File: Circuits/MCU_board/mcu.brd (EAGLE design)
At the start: 80 x 70 mm, 78 parts, among them IC1 RP111N331B-TR-FE, IC2 FT230XS, U1 TCA9548APWR, U2 USBLC6-2P6, U4 LSM9DS1, U5 STM32L452RECT6

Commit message: Separate a couple of MCU traces to use separate vias to avoid potential loop
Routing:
- net GND: track 143.2 -> 137.7 mm, vias 17 -> 18
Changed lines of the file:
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@@
 <?xml version="1.0" encoding="utf-8"?>
 <!DOCTYPE eagle SYSTEM "eagle.dtd">
-<eagle version="9.4.2">
+<eagle version="9.3.2">
 <drawing>
 <settings>
@@
 <attribute name="MEM" value="" x="61.4022" y="35.0262" size="1.778" layer="27" display="off"/>
 <attribute name="MFPN" value="STM32L476RCT6" x="61.4022" y="35.0262" size="1.778" layer="27" display="off"/>
+<attribute name="NAME" x="41.0822" y="44.5462" size="0.8128" layer="151" ratio="10" align="center"/>
 <attribute name="NAME" x="36.8822" y="48.1462" size="1.016" layer="25" font="vector" ratio="18" align="bottom-right"/>
-<attribute name="NAME" x="41.0822" y="44.5462" size="0.8128" layer="151" ratio="10" align="center"/>
 <attribute name="PARTNO" value="" x="61.4022" y="35.0262" size="1.778" layer="27" display="off"/>
 <attribute name="STATUS" value="" x="61.4022" y="35.0262" size="1.778" layer="27" display="off"/>
@@
 <wire x1="14.4726" y1="53.163" x2="16.687" y2="53.163" width="0.3048" layer="1"/>
 <wire x1="16.687" y1="53.163" x2="16.6878" y2="53.1622" width="0.1524" layer="1"/>
-<via x="41.0972" y="34.0106" extent="1-16" drill="0.35"/>
-<wire x1="44.3322" y1="36.8962" x2="44.3322" y2="34.8326" width="0.3048" layer="1"/>
-<wire x1="44.3322" y1="34.8326" x2="43.5102" y2="34.0106" width="0.3048" layer="1"/>
-<wire x1="41.0972" y1="34.0106" x2="43.5102" y2="34.0106" width="0.3048" layer="1"/>
+<via x="44.3322" y="33.9852" extent="1-16" drill="0.35"/>
 <wire x1="57.6084" y1="35.2672" x2="57.6084" y2="33.3768" width="0.3048" layer="1"/>
 <wire x1="57.6084" y1="33.3768" x2="57.6072" y2="33.3756" width="0.1524" layer="1"/>
@@
 <wire x1="21.4046" y1="29.4873" x2="19.0521" y2="29.4873" width="0.3048" layer="1"/>
 <wire x1="19.0521" y1="29.4873" x2="19.05" y2="29.4894" width="0.1524" layer="1"/>
-<wire x1="37.8322" y1="36.8962" x2="37.8322" y2="34.761" width="0.3048" layer="1"/>
-<wire x1="37.8322" y1="34.761" x2="38.5826" y2="34.0106" width="0.3048" layer="1"/>
-<wire x1="38.5826" y1="34.0106" x2="41.0972" y2="34.0106" width="0.3048" layer="1"/>
 <wire x1="42.8954" y1="25.3306" x2="42.8752" y2="25.3104" width="0.1524" layer="1"/>
 <wire x1="42.8752" y1="25.3104" x2="42.8752" y2="22.4028" width="0.3048" layer="1"/>
@@
 <wire x1="70.0532" y1="17.9832" x2="72.93233125" y2="18.5018375" width="0.3048" layer="1"/>
 <wire x1="69.84200625" y1="73.107125" x2="69.4182" y2="70.7898" width="0.3048" layer="1"/>
+<wire x1="44.3322" y1="36.8962" x2="44.3322" y2="33.9852" width="0.3048" layer="1"/>
+<via x="37.8322" y="33.9852" extent="1-16" drill="0.35"/>
+<wire x1="37.8322" y1="36.8962" x2="37.8322" y2="33.9852" width="0.3048" layer="1"/>
 </signal>
 <signal name="SWDIO">

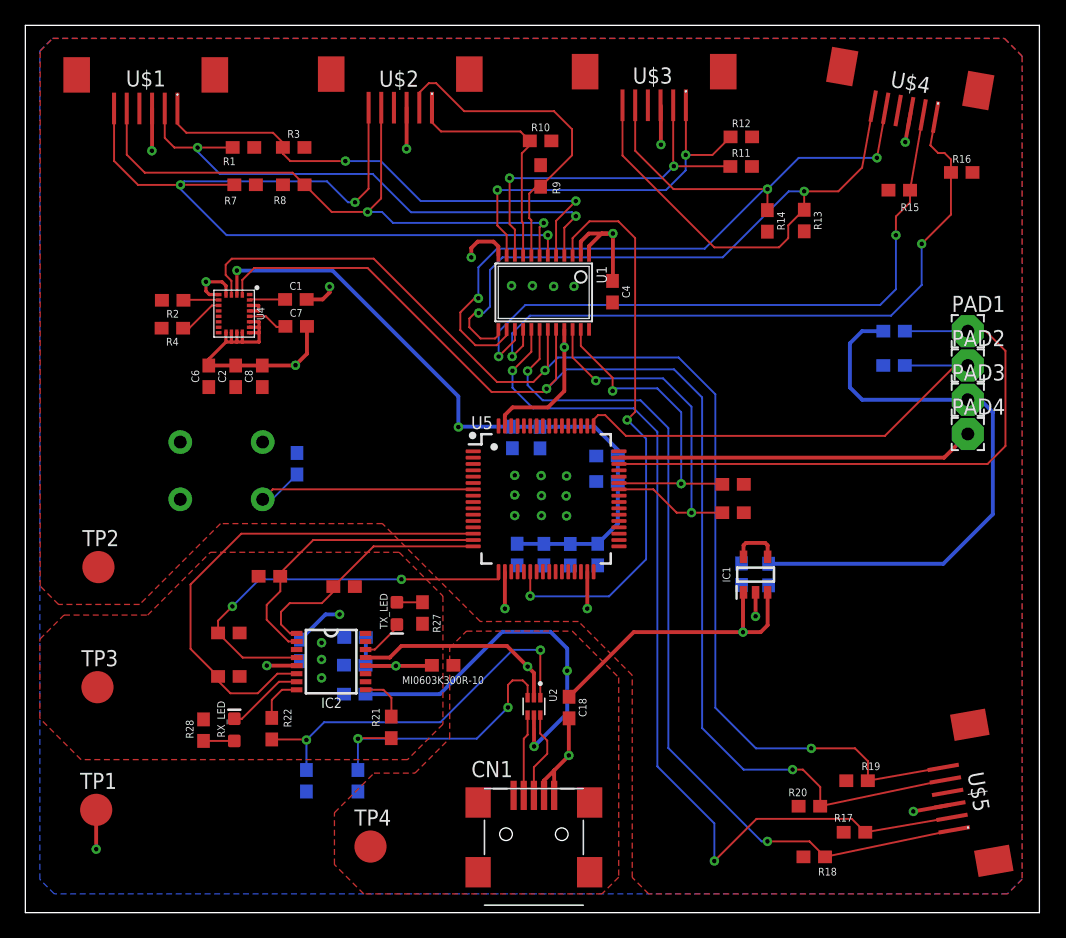
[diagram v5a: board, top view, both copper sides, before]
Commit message: Fixed silkscreen of components, Changed VCCIO plane
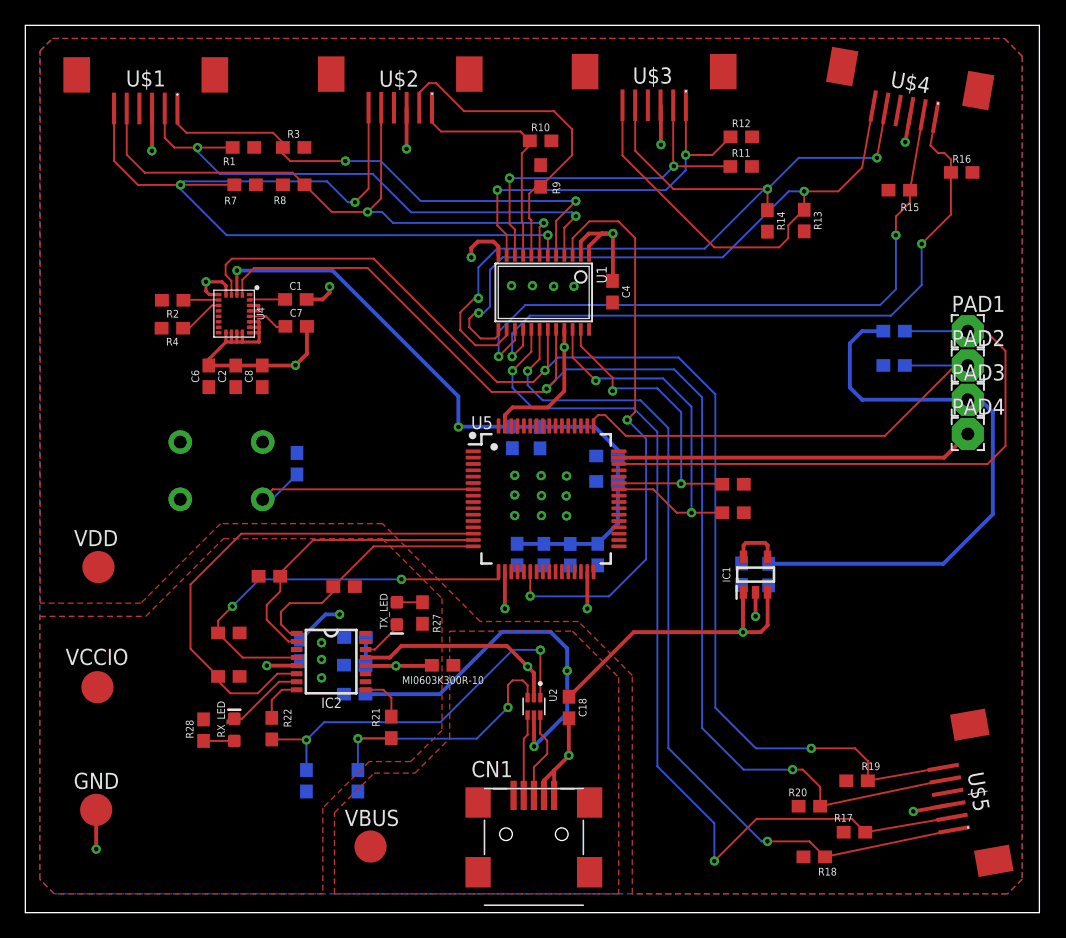
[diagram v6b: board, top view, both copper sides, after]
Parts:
- renumbered TP1 to GND, TP2 to VDD, TP3 to VCCIO, TP4 to VBUS
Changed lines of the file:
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@@
 <?xml version="1.0" encoding="utf-8"?>
 <!DOCTYPE eagle SYSTEM "eagle.dtd">
-<eagle version="9.3.2">
+<eagle version="9.4.2">
 <drawing>
 <settings>
@@
 <attribute name="MEM" value="" x="61.4022" y="35.0262" size="1.778" layer="27" display="off"/>
 <attribute name="MFPN" value="STM32L476RCT6" x="61.4022" y="35.0262" size="1.778" layer="27" display="off"/>
+<attribute name="NAME" x="36.8822" y="48.1462" size="1.016" layer="25" font="vector" ratio="18" align="bottom-right"/>
 <attribute name="NAME" x="41.0822" y="44.5462" size="0.8128" layer="151" ratio="10" align="center"/>
-<attribute name="NAME" x="36.8822" y="48.1462" size="1.016" layer="25" font="vector" ratio="18" align="bottom-right"/>
 <attribute name="PARTNO" value="" x="61.4022" y="35.0262" size="1.778" layer="27" display="off"/>
 <attribute name="STATUS" value="" x="61.4022" y="35.0262" size="1.778" layer="27" display="off"/>
@@
 <attribute name="VALUE" x="55.8292" y="43.0276" size="0.6096" layer="27" font="vector" ratio="20" align="top-center"/>
 </element>
-<element name="TP1" library="testpad" library_urn="urn:adsk.eagle:library:385" package="B2,54" package3d_urn="urn:adsk.eagle:package:27948/1" value="TPB2,54" x="5.588" y="18.1102" smashed="yes">
-<attribute name="NAME" x="4.318" y="19.7612" size="1.27" layer="25" ratio="10"/>
+<element name="GND" library="testpad" library_urn="urn:adsk.eagle:library:385" package="B2,54" package3d_urn="urn:adsk.eagle:package:27948/1" value="TPB2,54" x="5.588" y="18.1102" smashed="yes">
+<attribute name="NAME" x="3.81" y="19.7612" size="1.27" layer="25" ratio="10"/>
 <attribute name="TP_SIGNAL_NAME" value="" x="5.588" y="18.1102" size="1.778" layer="27" display="off"/>
 <attribute name="VALUE" x="4.318" y="16.7132" size="0.0254" layer="27"/>
 </element>
-<element name="TP2" library="testpad" library_urn="urn:adsk.eagle:library:385" package="B2,54" package3d_urn="urn:adsk.eagle:package:27948/1" value="TPB2,54" x="5.7658" y="37.2618" smashed="yes">
-<attribute name="NAME" x="4.4958" y="38.9128" size="1.27" layer="25" ratio="10"/>
+<element name="VDD" library="testpad" library_urn="urn:adsk.eagle:library:385" package="B2,54" package3d_urn="urn:adsk.eagle:package:27948/1" value="TPB2,54" x="5.7658" y="37.2618" smashed="yes">
+<attribute name="NAME" x="3.8354" y="38.9128" size="1.27" layer="25" ratio="10"/>
 <attribute name="TP_SIGNAL_NAME" value="" x="5.7658" y="37.2618" size="1.778" layer="27" display="off"/>
 <attribute name="VALUE" x="4.4958" y="35.8648" size="0.0254" layer="27"/>
 </element>
-<element name="TP3" library="testpad" library_urn="urn:adsk.eagle:library:385" package="B2,54" package3d_urn="urn:adsk.eagle:package:27948/1" value="TPB2,54" x="5.6896" y="27.7876" smashed="yes">
-<attribute name="NAME" x="4.4196" y="29.4386" size="1.27" layer="25" ratio="10"/>
+<element name="VCCIO" library="testpad" library_urn="urn:adsk.eagle:library:385" package="B2,54" package3d_urn="urn:adsk.eagle:package:27948/1" value="TPB2,54" x="5.6896" y="27.7876" smashed="yes">
+<attribute name="NAME" x="3.175" y="29.5402" size="1.27" layer="25" ratio="10"/>
 <attribute name="TP_SIGNAL_NAME" value="" x="5.6896" y="27.7876" size="1.778" layer="27" display="off"/>
 <attribute name="VALUE" x="4.4196" y="26.3906" size="0.0254" layer="27"/>
 </element>
-<element name="TP4" library="testpad" library_urn="urn:adsk.eagle:library:385" package="B2,54" package3d_urn="urn:adsk.eagle:package:27948/1" value="TPB2,54" x="27.2288" y="15.2146" smashed="yes">
-<attribute name="NAME" x="25.9588" y="16.8656" size="1.27" layer="25" ratio="10"/>
+<element name="VBUS" library="testpad" library_urn="urn:adsk.eagle:library:385" package="B2,54" package3d_urn="urn:adsk.eagle:package:27948/1" value="TPB2,54" x="27.2288" y="15.2146" smashed="yes">
+<attribute name="NAME" x="25.1968" y="16.8402" size="1.27" layer="25" ratio="10"/>
 <attribute name="TP_SIGNAL_NAME" value="" x="27.2288" y="15.2146" size="1.778" layer="27" display="off"/>
 <attribute name="VALUE" x="25.9588" y="13.8176" size="0.0254" layer="27"/>
@@
 <wire x1="42.8954" y1="25.3306" x2="42.8752" y2="25.3104" width="0.1524" layer="1"/>
 <wire x1="42.8752" y1="25.3104" x2="42.8752" y2="22.4028" width="0.3048" layer="1"/>
-<contactref element="TP1" pad="TP"/>
+<contactref element="GND" pad="TP"/>
 <via x="5.588" y="15.0114" extent="1-16" drill="0.35"/>
 <wire x1="5.588" y1="15.0114" x2="5.588" y2="18.1102" width="0.3048" layer="1"/>
@@
 <contactref element="R29" pad="2"/>
 <contactref element="R30" pad="2"/>
-<contactref element="TP2" pad="TP"/>
+<contactref element="VDD" pad="TP"/>
 <polygon width="0.1524" layer="1">
 <vertex x="2.159" y="78.9686"/>
@@
 <vertex x="78.6384" y="12.6238"/>
 <vertex x="77.4954" y="11.4808"/>
-<vertex x="49.1744" y="11.4808"/>
-<vertex x="47.879" y="12.7762"/>
+<vertex x="47.879" y="11.4808"/>
 <vertex x="47.879" y="28.7274"/>
 <vertex x="43.6372" y="32.9692"/>
@@
 <vertex x="28.1686" y="40.6908"/>
 <vertex x="15.3924" y="40.6908"/>
-<vertex x="9.017" y="34.3154"/>
-<vertex x="2.6162" y="34.3154"/>
-<vertex x="1.1684" y="35.7632"/>
+<vertex x="9.1186" y="34.417"/>
+<vertex x="1.1684" y="34.417"/>
 <vertex x="1.1684" y="77.978"/>
 </polygon>
@@
 <wire x1="41.4274" y1="32.1564" x2="42.7482" y2="30.8356" width="0.3048" layer="16"/>
 <wire x1="42.7482" y1="30.8356" x2="42.7482" y2="29.083" width="0.3048" layer="16"/>
-<contactref element="TP4" pad="TP"/>
+<contactref element="VBUS" pad="TP"/>
 <polygon width="0.1524" layer="1">
 <vertex x="43.1546" y="32.2072"/>
 <vertex x="46.8122" y="28.5496"/>
-<vertex x="46.8122" y="12.8016"/>
-<vertex x="45.4914" y="11.4808"/>
-<vertex x="26.6954" y="11.4808"/>
-<vertex x="24.384" y="13.7922"/>
+<vertex x="46.8122" y="11.4808"/>
+<vertex x="24.384" y="11.4808"/>
 <vertex x="24.384" y="17.8816"/>
 <vertex x="27.5082" y="21.0058"/>
 <vertex x="30.734" y="21.0058"/>
 <vertex x="33.4772" y="23.749"/>
-<vertex x="33.4772" y="30.8864"/>
-<vertex x="34.798" y="32.2072"/>
+<vertex x="33.4772" y="32.2072"/>
 </polygon>
 </signal>
@@
 <wire x1="21.6918" y1="31.5406" x2="23.6792" y2="33.528" width="0.3048" layer="16"/>
 <wire x1="23.6792" y1="33.528" x2="24.7904" y2="33.528" width="0.3048" layer="16"/>
-<contactref element="TP3" pad="TP"/>
+<contactref element="VCCIO" pad="TP"/>
 <polygon width="0.1524" layer="1">
-<vertex x="9.652" y="33.4772"/>
-<vertex x="14.605" y="38.4302"/>
-<vertex x="29.4894" y="38.4302"/>
-<vertex x="32.9438" y="34.9758"/>
-<vertex x="32.9438" y="24.8666"/>
-<vertex x="30.1498" y="22.0726"/>
-<vertex x="4.3942" y="22.0726"/>
-<vertex x="1.143" y="25.3238"/>
-<vertex x="1.143" y="31.5722"/>
-<vertex x="3.048" y="33.4772"/>
+<vertex x="1.143" y="33.3756"/>
+<vertex x="9.4996" y="33.3756"/>
+<vertex x="15.621" y="39.497"/>
+<vertex x="28.1686" y="39.497"/>
+<vertex x="32.8676" y="34.798"/>
+<vertex x="32.8676" y="24.384"/>
+<vertex x="30.4038" y="21.9202"/>
+<vertex x="27.1272" y="21.9202"/>
+<vertex x="23.4696" y="18.2626"/>
+<vertex x="23.4696" y="11.4808"/>
+<vertex x="2.286" y="11.4808"/>
+<vertex x="1.143" y="12.6238"/>
 </polygon>
 </signal>

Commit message: Add silkscreen component names
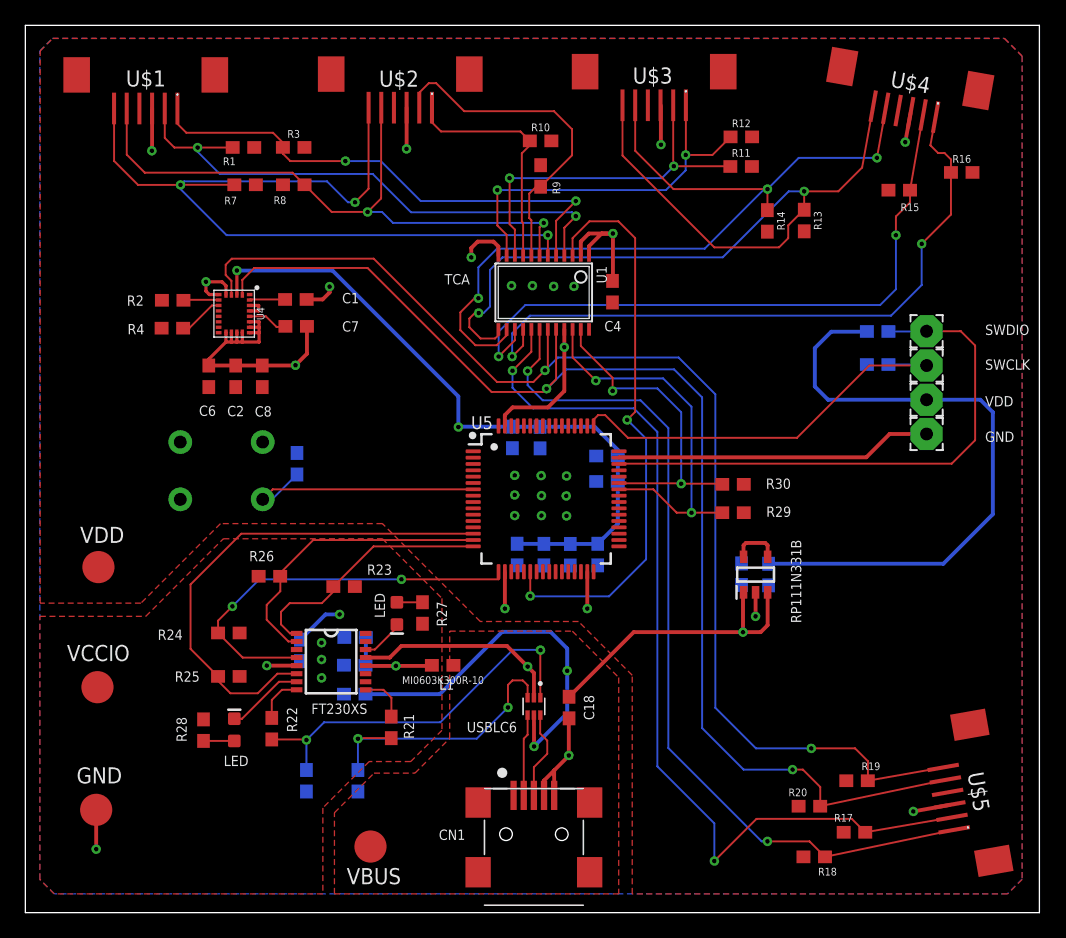
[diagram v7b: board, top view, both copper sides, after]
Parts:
- moved PAD2 3.25 mm to (71.1, 53.2)
- moved PAD3 3.25 mm to (71.1, 50.5)
- moved PAD4 3.25 mm to (71.1, 47.8)
- moved PAD1 3.25 mm to (71.1, 55.9)
- moved R5 1.30 mm to (67.2, 53.2)
- moved R6 1.30 mm to (67.2, 55.8)
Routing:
- net SWCLK: track 38.1 -> 33.1 mm
- net VDD: track 105.4 -> 109.4 mm
- net SWDIO: track 47.2 -> 43.7 mm
- net GND: track 137.7 -> 134.4 mm
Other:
- board text added: "FT230XS"
- board text added: "GND"
- board text added: "L1"
- board text added: "LED"
- board text added: "MCU BOARD V1 BEN WU TEJASVI JODHKA GAUNTLET"
- board text added: "R23"
- board text added: "R24"
- board text added: "R25"
- board text added: "R26"
- board text added: "R29"
- board text added: "R30"
- board text added: "RP111N331B"
- board text added: "SWCLK"
- board text added: "SWDIO"
- board text added: "TCA"
- board text added: "USBLC6"
- board text added: "VDD"
